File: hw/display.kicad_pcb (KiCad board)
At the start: 2 copper layers, 81.4 x 40.1 mm, 45 parts, among them J101 AMPSEAL_8_POS_VERT_BLACK_SEAL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, J301 HEADER_MOLEX_54104-4031, J401 ARM_JTAG_SWD_HEADER_10_PINSMD, U101 MCP2551_SOIC8, U301 FT812, U302 LED_DRIVER_MIC2289, U401 LPC1549JBD64, U501 WINDBOND_W25Q128JVSIQ_SOIC8_W, X401 XTAL_7A-12.000MAAJ-T, X402 XTAL_ABS25-32.768KHZ-T

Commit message: 1.7.0 pcb created, not yet ordered
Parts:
- removed C305: 100nF, kemet:0603
- removed C306: T491D226K035AT, kemet:7343
- removed F101: FUSE_MC36211_350MA, usevolt:FUSE_MC36211
- added C303: 100nF, kemet:0603, F.Cu at (169.4, 107.0)
- added C304: CAP_EEE-FK1H470P, usevolt:CAP_EEE-FK1H470P, F.Cu at (167.6, 96.4)
- added D301: DIODE_RS07J-GS18, usevolt:DO219AB, F.Cu at (171.6, 103.3)
- added F202: FUSE_MC36211_350MA, usevolt:FUSE_MC36211, F.Cu at (128.2, 86.9)
- added J302: HEADER_MOLEX_52207-0433, usevolt:HEADER_MOLEX_52207-0433, B.Cu at (103.6, 103.8)
- C201: value T491D226K035AT -> CAP_EEE-FK1H470P; footprint kemet:7343 -> usevolt:CAP_EEE-FK1H470P
- R302: value R_2OHM -> R_0.33OHM
- U302: value LED_DRIVER_MIC2289 -> AL8805W5-7_LED_DRIVER; footprint usevolt:MLF_8 -> usevolt:SOT-25
- moved G*** 87.7 mm to (194.9, 91.6)
- moved C202 45.8 mm to (154.1, 106.0), turned to 180 degrees
- moved U501 31.1 mm to (198.3, 79.0), turned to 90 degrees
- moved L201 30.3 mm to (151.6, 97.4), turned to 0 degrees
- moved J301 27.0 mm to (188.7, 107.7)
- moved C501 26.6 mm to (196.3, 73.2), turned to 180 degrees
- moved R301 25.6 mm to (179.8, 89.5)
- moved C302 25.5 mm to (181.4, 89.5)
- moved U301 25.3 mm to (183.2, 96.3)
- moved C205 25.1 mm to (155.9, 89.2), turned to 270 degrees
- moved C301 24.7 mm to (176.9, 95.6)
- moved VR2 23.3 mm to (152.7, 89.2), turned to 90 degrees
- moved C201 22.3 mm to (113.8, 104.3), turned to 90 degrees
- moved C408 15.4 mm to (167.7, 75.5), turned to 90 degrees
- moved C405 15.0 mm to (177.5, 78.3)
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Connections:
- F1 pad P$1: VDD -> /power_supply/VIN
- F201 pad P$1: VDD -> /power_supply/VIN
- F201 pad P$2: (no net) -> VEE
- J101 pad 1: VDD -> /power_supply/VIN
- J101 pad 6: Net-(F101-PadP$1) -> (no net)
- J301 pad 37: /TFT-LCD/XR -> (no net)
- J301 pad 38: /TFT-LCD/YD -> (no net)
- J301 pad 39: /TFT-LCD/XL -> (no net)
- J301 pad 40: /TFT-LCD/YU -> (no net)
- L301 pad 1: +5V -> Net-(L301-Pad1)
- L301 pad 2: Net-(L301-Pad2) -> /TFT-LCD/LED-
- R302 pad 1: /TFT-LCD/LED- -> VEE
- R302 pad 2: GND -> /TFT-LCD/LED+
- U301 pad 23: /TFT-LCD/XR -> /TFT-LCD/XL
- U301 pad 25: /TFT-LCD/XL -> /TFT-LCD/XR
- U302 pad 1: /TFT-LCD/LED+ -> Net-(L301-Pad1)
- U302 pad 2: +5V -> GND
- U302 pad 4: GND -> /TFT-LCD/LED+
- U302 pad 5: (no net) -> VEE
- U401 pad P$1: /lpc1549/FLASH_MOSI -> (no net)
- U401 pad P$38: /TFT-LCD/CS -> (no net)
- U401 pad P$5: (no net) -> /Sheet59C68157/CS
- U401 pad P$51: /lpc1549/LCD_MOSI -> /lpc1549/LCD_PD
- U401 pad P$53: /lpc1549/LCD_MISO -> /TFT-LCD/CS
- U401 pad P$54: /lpc1549/LCD_PD -> (no net)
- U401 pad P$58: /lpc1549/LCD_SCK -> /lpc1549/LCD_MOSI
- U401 pad P$6: (no net) -> /lpc1549/FLASH_MISO
- U401 pad P$61: /Sheet59C68157/CS -> /lpc1549/LCD_MISO
- U401 pad P$62: /Sheet59C68157/CLK -> /lpc1549/LCD_SCK
- U401 pad P$63: /lpc1549/FLASH_MISO -> (no net)
- U401 pad P$7: (no net) -> /lpc1549/FLASH_MOSI
- U401 pad P$8: (no net) -> /Sheet59C68157/CLK
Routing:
- net VEE: track 0.00 -> 118.8 mm
- net +5V: track 165.2 -> 65.3 mm, vias 4 -> 0
- net GND: track 472.4 -> 546.4 mm
- net /TFT-LCD/XL: track 13.2 -> 82.8 mm, vias 0 -> 1
- net (no net): track 69.5 -> 0.00 mm, vias 4 -> 0
- net /TFT-LCD/YU: track 11.1 -> 77.9 mm, vias 0 -> 1
- net /TFT-LCD/YD: track 15.4 -> 81.3 mm, vias 0 -> 1
- net /TFT-LCD/XR: track 17.7 -> 79.9 mm, vias 0 -> 1
- net +3V3: track 195.7 -> 150.1 mm, vias 8 -> 0
- net /TFT-LCD/LED-: track 5.01 -> 40.1 mm
- net /TFT-LCD/CS: track 33.0 -> 6.92 mm, vias 2 -> 0
- net /TFT-LCD/LED+: track 21.5 -> 44.5 mm
- net /Sheet59C68157/CS: track 26.1 -> 4.86 mm
- net /lpc1549/FLASH_MISO: track 27.0 -> 6.32 mm
- net /lpc1549/LCD_SCK: track 24.8 -> 9.21 mm
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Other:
- board size 81.4 x 40.1 mm -> 100 x 40.1 mm
- board text added: "Usevolt Oy uw_display 1.7.0"
- board text removed: "Usevolt Oy uv0a-hds"

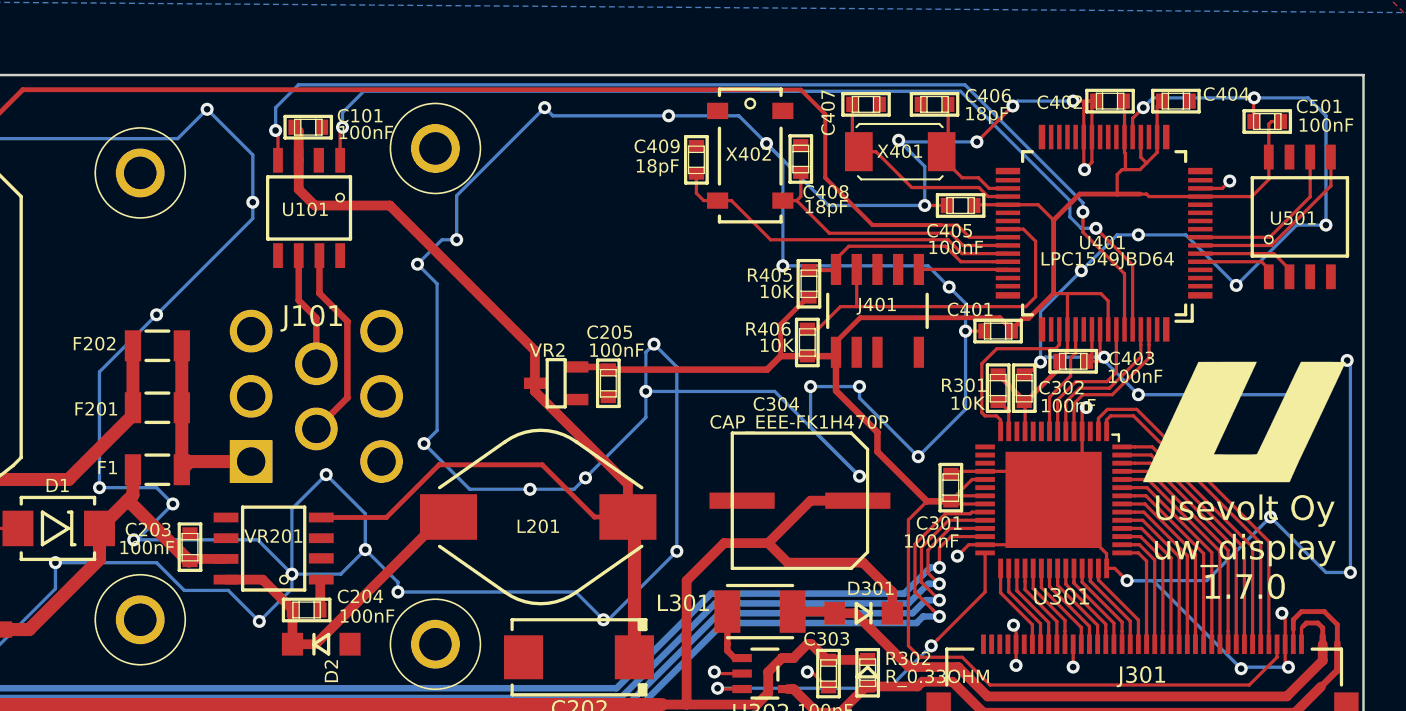
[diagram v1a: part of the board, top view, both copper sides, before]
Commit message: uw180s grab times adjustable
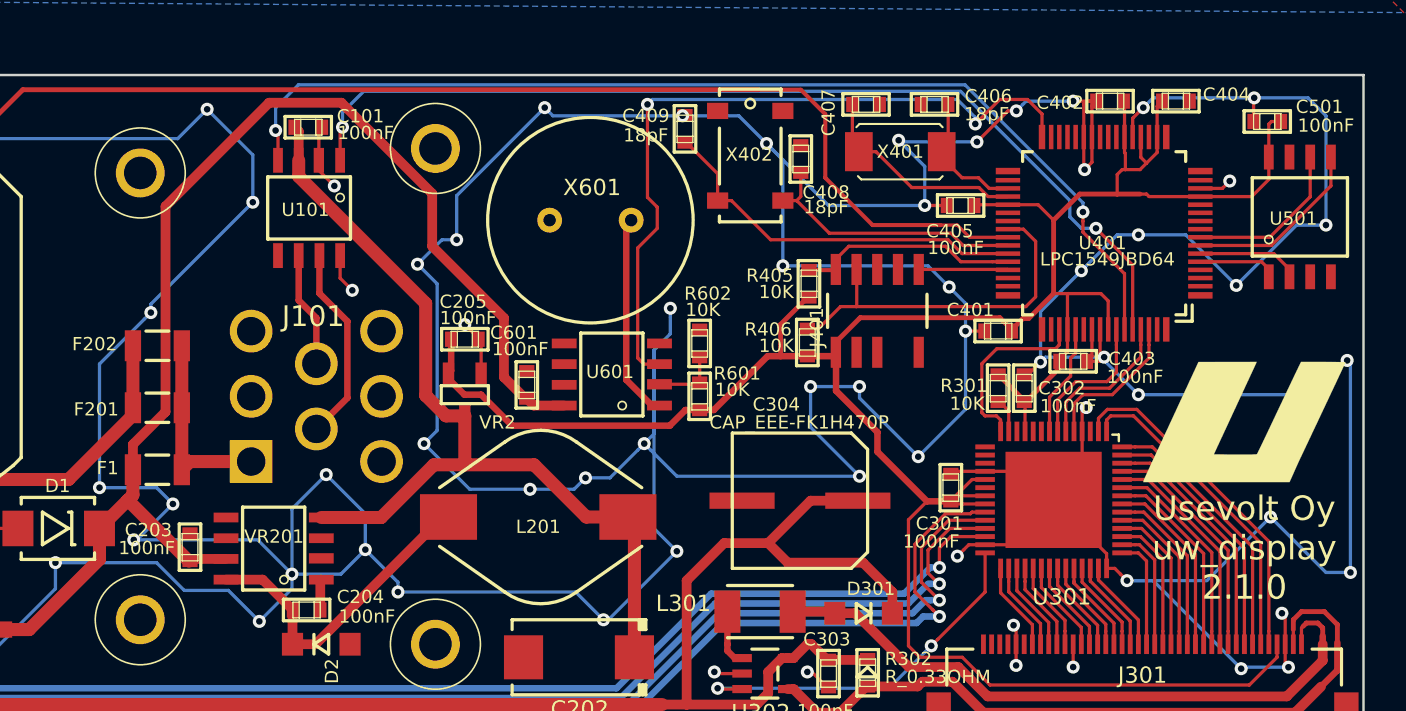
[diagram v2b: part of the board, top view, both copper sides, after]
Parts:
- added C601: 100nF, kemet:0603, F.Cu at (150.9, 89.3)
- added R601: 10K, multicomp:0603, F.Cu at (161.5, 90.0)
- added R602: 10K, multicomp:0603, F.Cu at (161.5, 86.8)
- added U601: OPAMP_LM358DT, usevolt:SOIC8, F.Cu at (156.1, 88.7)
- added X601: BUZZER_PKM13EPYH4002-B0, usevolt:BUZZER_PKM13EPYH4002-B0, F.Cu at (154.8, 79.2)
- moved C205 9.20 mm to (147.1, 86.5), turned to 0 degrees
- moved VR2 5.64 mm to (147.1, 89.9), turned to 180 degrees
- moved J401 2.83 mm to (172.4, 84.8)
- moved C409 2.02 mm to (160.6, 73.6)
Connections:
- U401 pad P$32: (no net) -> /lpc1549/BUZZER
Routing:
- net VDD: track 23.1 -> 78.9 mm
- net /lpc1549/BUZZER: track 0.00 -> 45.4 mm, vias 0 -> 2
- net +3V3: track 150.1 -> 163.1 mm
- net Net-(U601-Pad1): track 0.00 -> 12.6 mm
- net GND: track 546.4 -> 558.2 mm, vias 70 -> 73
- net +5V: track 65.3 -> 55.9 mm
- net Net-(R601-Pad1): track 0.00 -> 4.07 mm
- net Net-(C409-Pad1): track 21.8 -> 23.6 mm
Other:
- board text added: "Usevolt Oy uw_display 2.1.0"
- board text removed: "Usevolt Oy uw_display 1.7.0"

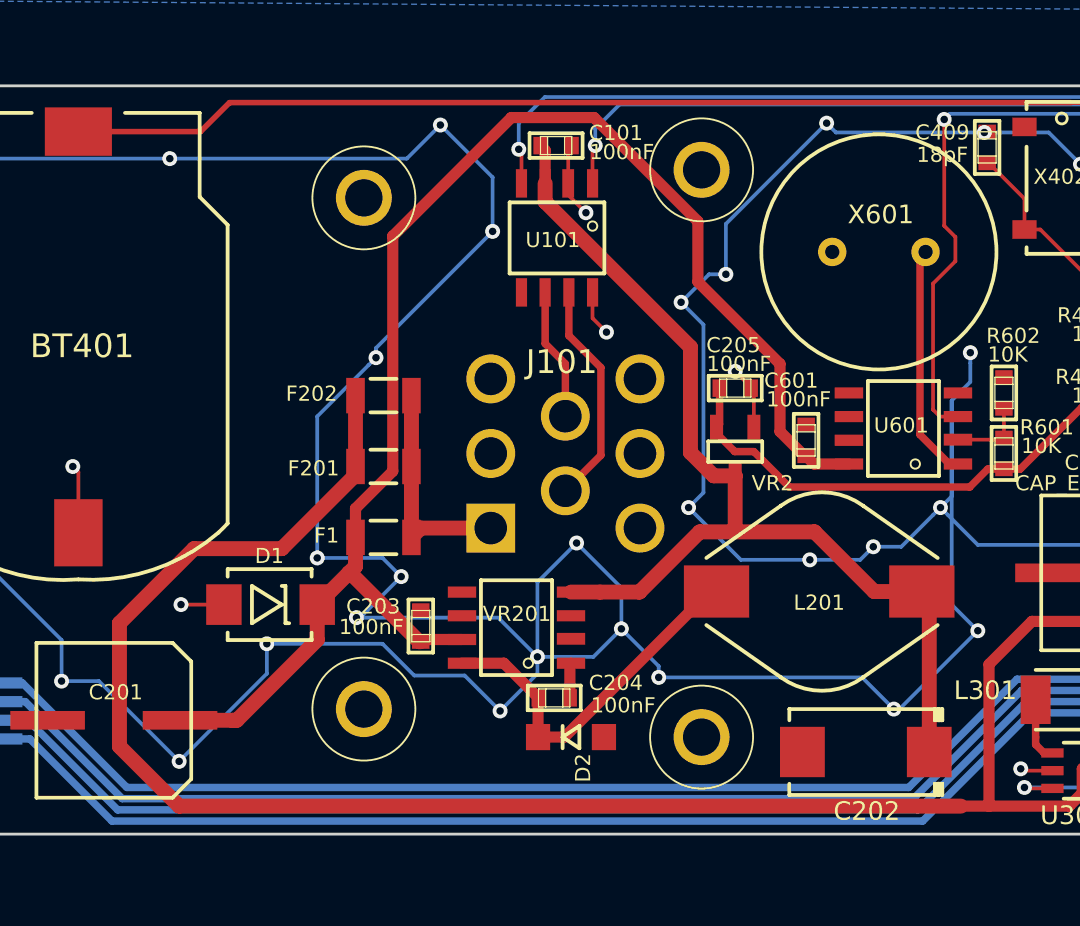
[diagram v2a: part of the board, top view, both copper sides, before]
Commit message: hw 2.1.0 with LPC1549 & FT812 ordered from seeed
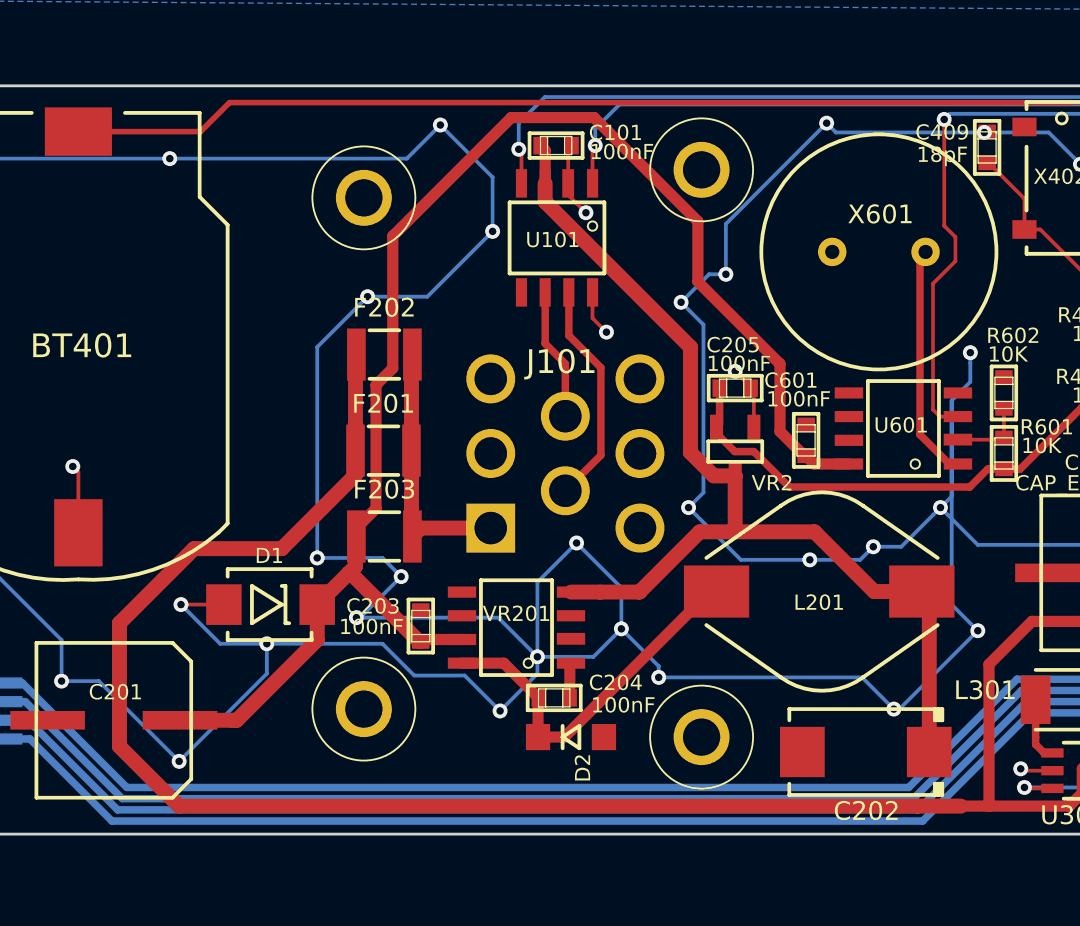
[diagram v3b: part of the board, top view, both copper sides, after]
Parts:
- removed F1: FUSE_MC36211_350MA, usevolt:FUSE_MC36211
- added F203: FUSE_0ZCH0075AF2E, usevolt:1210, F.Cu at (128.3, 94.5)
- F201, F202: value FUSE_MC36211_350MA -> FUSE_0ZCH0075AF2E; footprint usevolt:FUSE_MC36211 -> usevolt:1210
- moved F202 2.20 mm to (128.3, 84.7)
- moved F201 0.85 mm to (128.2, 89.8)
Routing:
- net GND: track 558.2 -> 565.5 mm
- net /power_supply/VIN: track 12.1 -> 16.0 mm
- net VEE: track 118.8 -> 121.1 mm

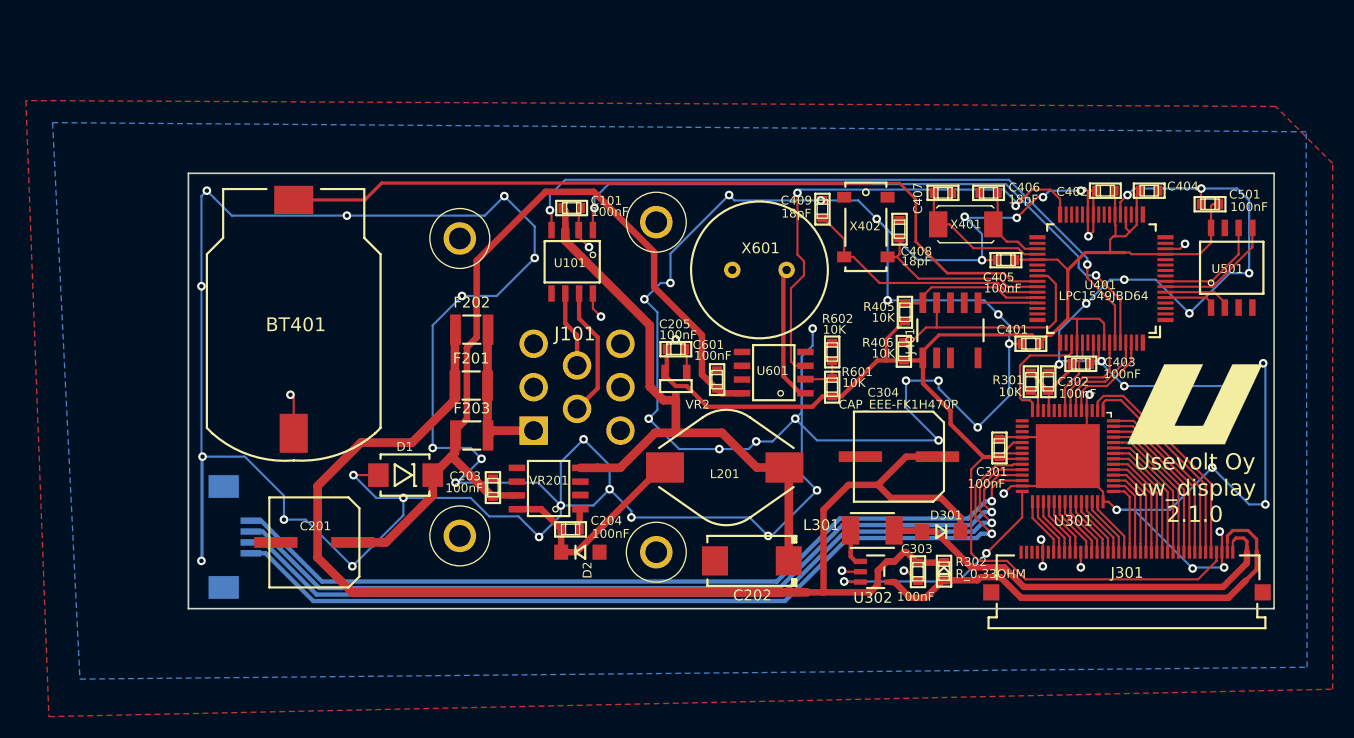
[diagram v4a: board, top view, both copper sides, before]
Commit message: working rtc module for LPC1549
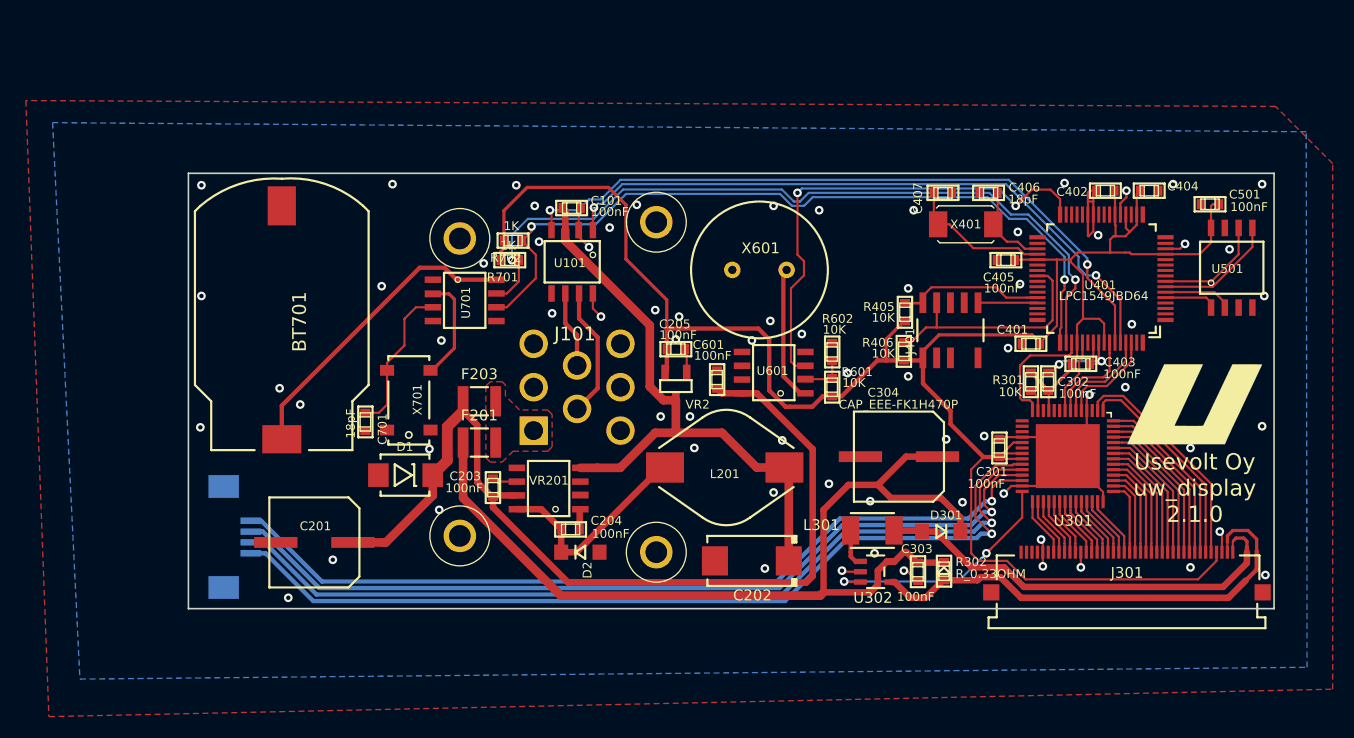
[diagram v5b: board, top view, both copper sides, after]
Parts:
- removed BT401: BATTERY_HOLDER_CH7410-2032LFSMD, usevolt:BATTERY_HOLDER_CH7410-2032LF
- removed C408, C409: 18pF, kemet:0603
- removed F202: FUSE_0ZCH0075AF2E, usevolt:1210
- removed X402: XTAL_ABS25-32.768KHZ-T, usevolt:XTAL_32.768KHZ-T
- added BT701: BATTERY_HOLDER_CH7410-2032LFSMD, usevolt:BATTERY_HOLDER_CH7410-2032LF, F.Cu at (110.8, 73.3)
- added C701: 18pF, kemet:0603, F.Cu at (118.5, 93.2)
- added R701: 1K, yageo:0603, F.Cu at (131.8, 78.3)
- added R702: 1K, yageo:0603, F.Cu at (132.1, 76.5)
- added U701: RTC_S-35390A-J8T1G, usevolt:SOIC8, F.Cu at (127.6, 82.0)
- added X701: XTAL_ABS25-32.768KHZ-T, usevolt:XTAL_32.768KHZ-T, F.Cu at (122.5, 91.2)
- moved F201 5.30 mm to (129.0, 95.1)
- moved F203 3.23 mm to (129.0, 91.3)
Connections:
- U401 pad P$41: Net-(BT401-Pad+) -> (no net)
- U401 pad P$42: Net-(C408-Pad1) -> (no net)
- U401 pad P$43: Net-(C409-Pad1) -> (no net)
- U401 pad P$49: (no net) -> /lpc1549/RTC_SCL
- U401 pad P$50: (no net) -> /lpc1549/RTC_SDA
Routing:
- net GND: track 565.5 -> 72.7 mm, vias 73 -> 72
- net Net-(BT401-Pad+): track 75.2 -> 0.00 mm
- net /lpc1549/RTC_SDA: track 0.00 -> 72.3 mm, vias 0 -> 2
- net /lpc1549/RTC_SCL: track 0.00 -> 71.9 mm, vias 0 -> 2
- net +3V3: track 163.1 -> 203.7 mm
- net VEE: track 121.1 -> 86.3 mm
- net Net-(BT701-Pad+): track 0.00 -> 28.6 mm
- net Net-(C409-Pad1): track 23.6 -> 0.00 mm
- net Net-(C408-Pad1): track 16.8 -> 0.00 mm
- net /power_supply/VIN: track 16.0 -> 0.00 mm
- net Net-(C701-Pad1): track 0.00 -> 13.9 mm
- net Net-(U701-Pad2): track 0.00 -> 9.73 mm
- net VDD: track 78.9 -> 86.7 mm
- net /lpc1549/CAN_RX: track 65.2 -> 64.4 mm
- added copper zone on F.Cu, net /power_supply/VIN
